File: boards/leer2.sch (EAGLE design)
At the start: 76 parts, among them IC2 7805DT, Q1 BC846BSMD, Q2 BC846BSMD, Q3 BC846BSMD, Q4 BC846BSMD, Q5 BC846BSMD, Q6 BC846BSMD, Q7 BC846BSMD, Q8 BC846BSMD

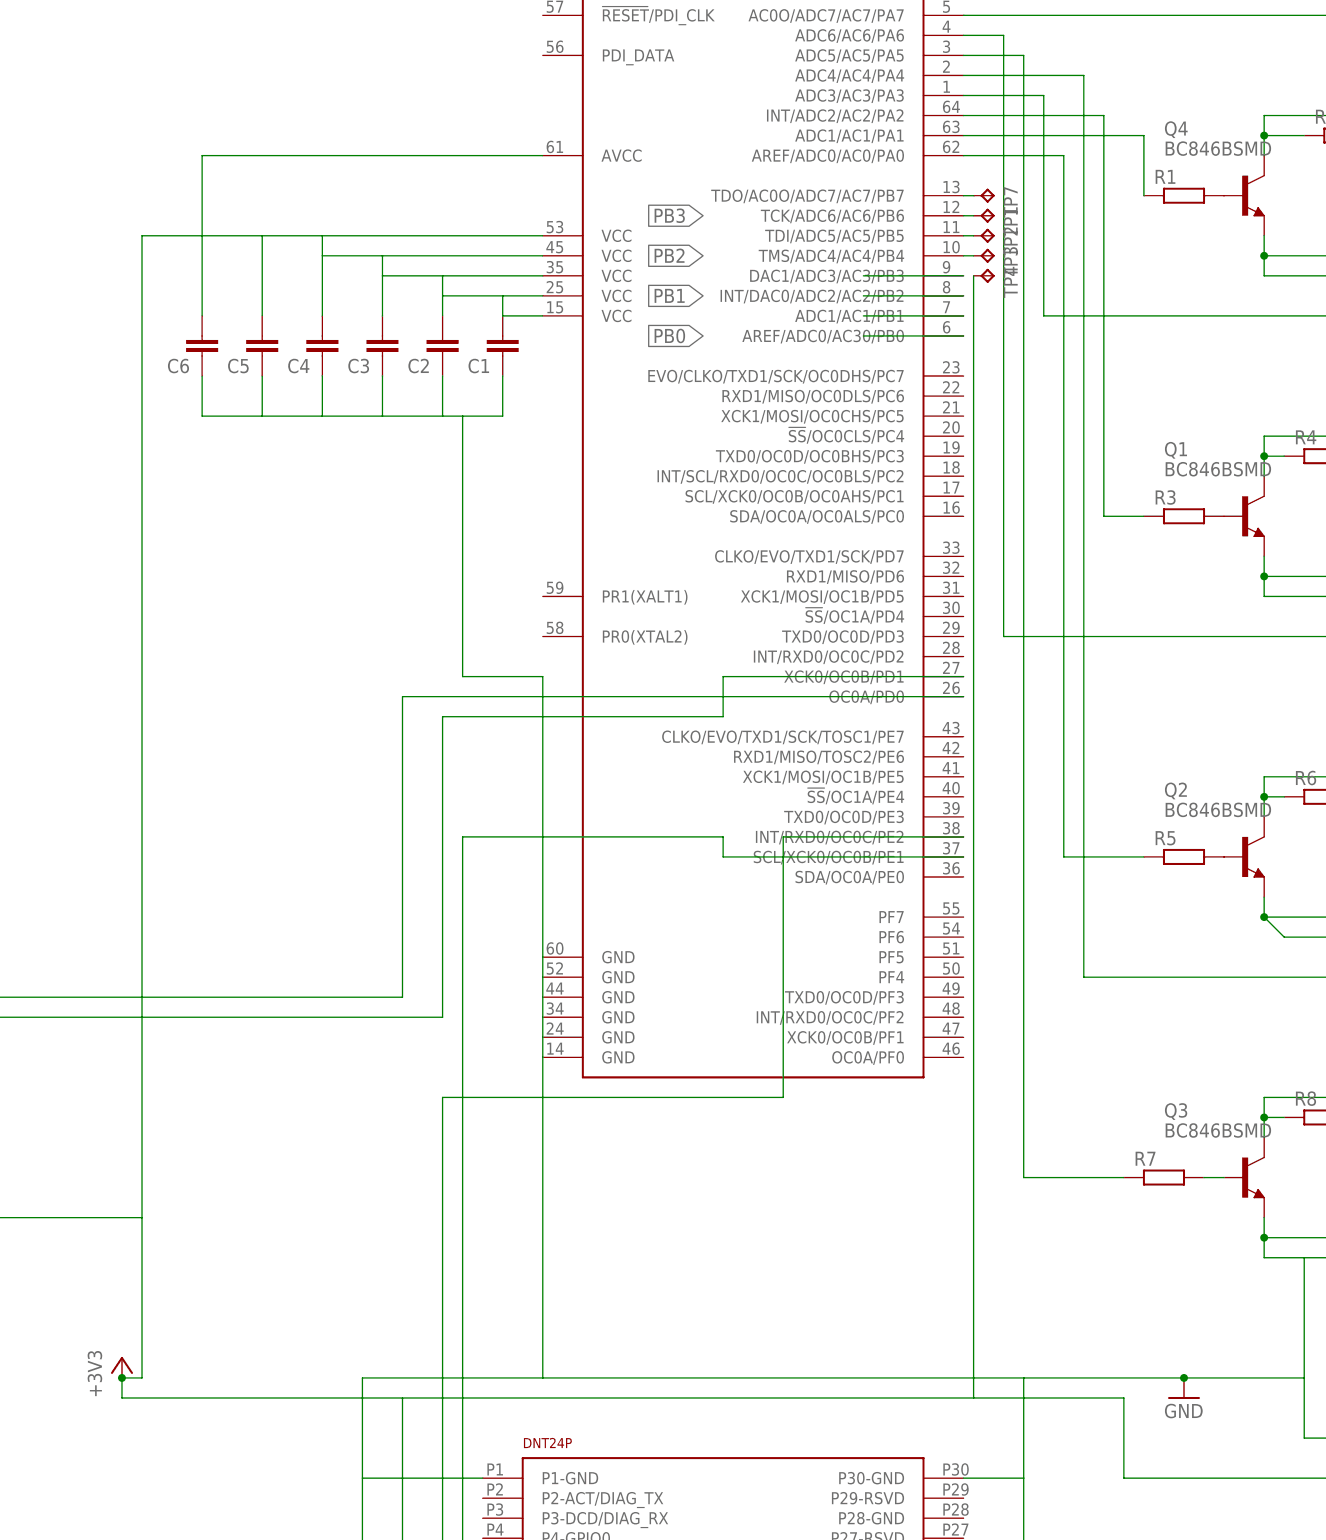
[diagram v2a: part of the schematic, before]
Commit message: Added Barometer
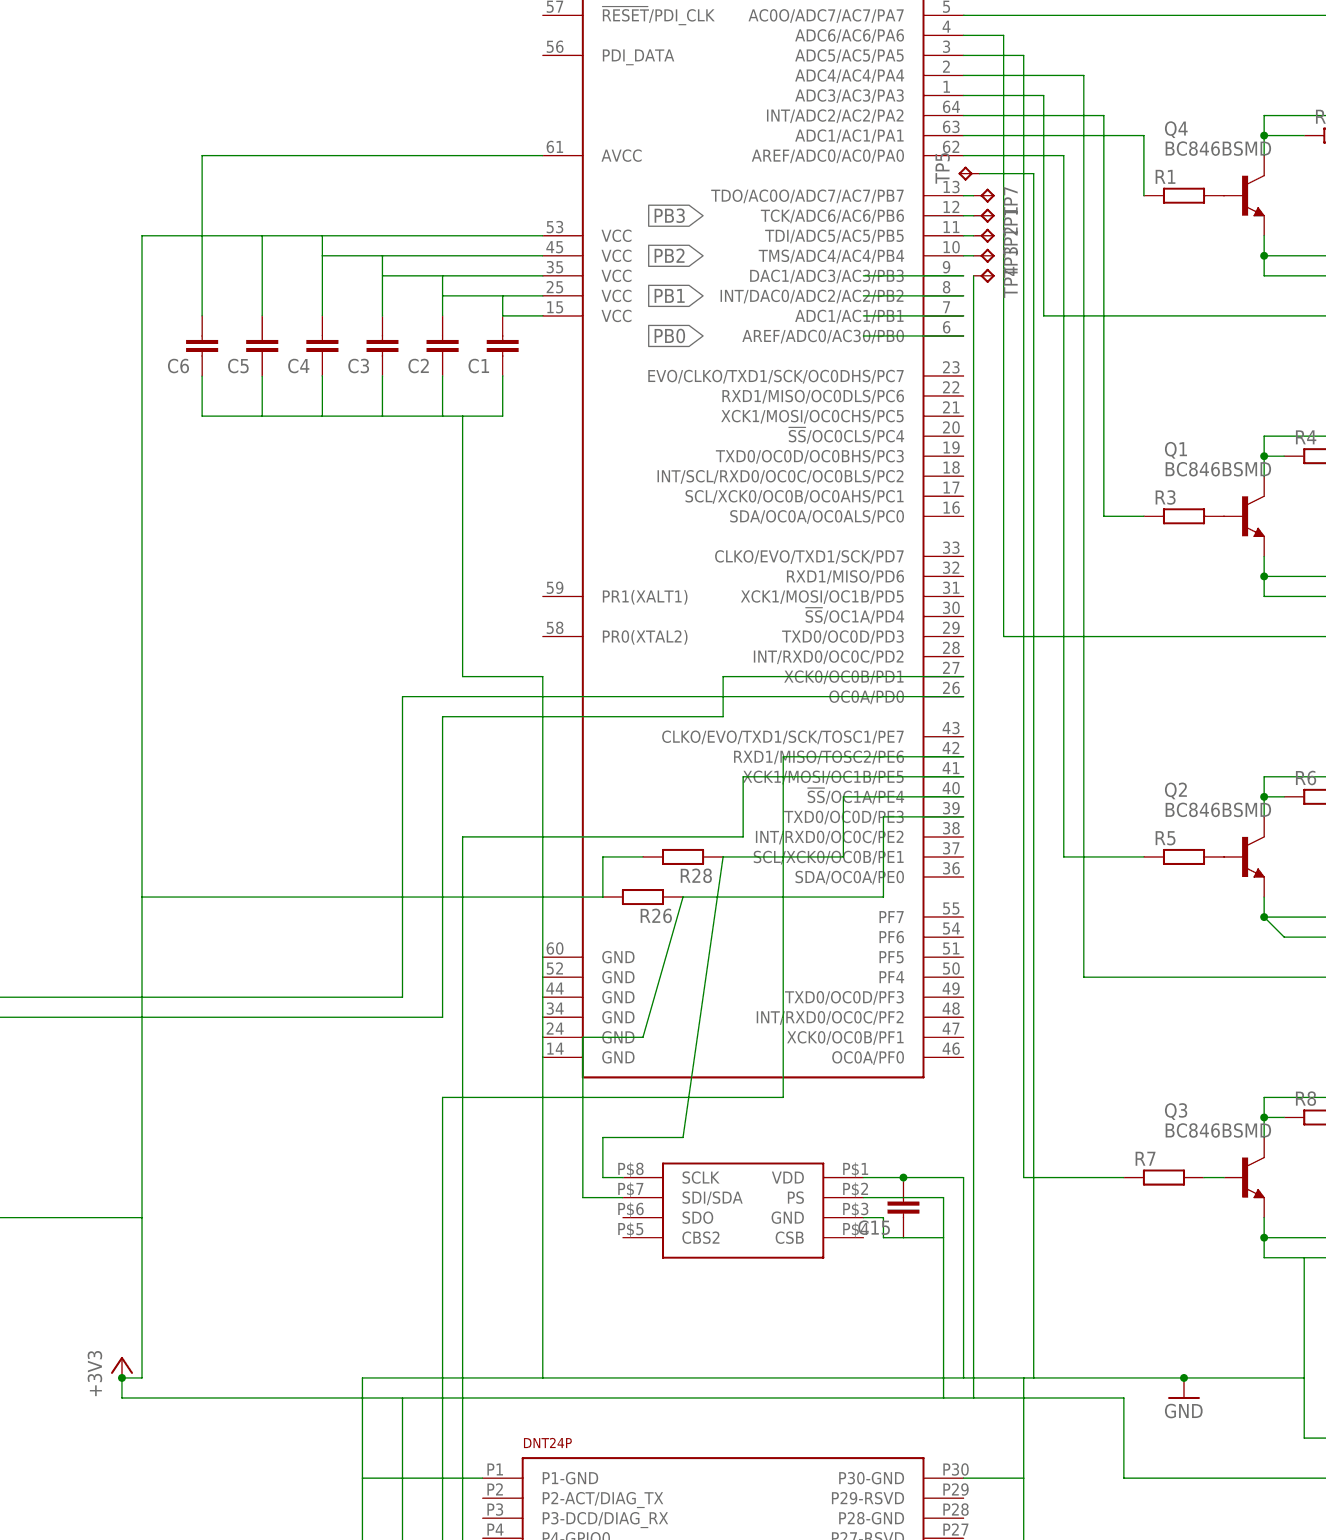
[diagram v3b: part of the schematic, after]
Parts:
- added C15: (no value), eagle-ltspice:CC0603
- added R26, R28: (no value), eagle-ltspice:RR0603
- added TP5: TPTP08R, testpad:TPTP08R
- added U$2: MS5611, ms5611:MS5611
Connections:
- new net N$46: IC3.!SS!/OC1A/PE4, R28.1, U$2.SCLK
- new net N$47: IC3.TXD0/OC0D/PE3, R26.1, U$2.SDI/SDA
- net +3V3: now also C15.1, R26.2, R28.2, U$2.GND, U$2.PS
- net GND: now also C15.2, TP5.TP, U$2.VDD
- net N$33: now also IC3.XCK1/MOSI/OC1B/PE5; no longer IC3.SCL/XCK0/OC0B/PE1
- net N$36: now also IC3.RXD1/MISO/TOSC2/PE6; no longer IC3.INT/RXD0/OC0C/PE2
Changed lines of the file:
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@@
 <?xml version="1.0" encoding="utf-8"?>
 <!DOCTYPE eagle SYSTEM "eagle.dtd">
-<eagle version="6.5.0">
+<eagle version="6.4">
 <drawing>
 <settings>
@@
 <layers>
 <layer number="1" name="Top" color="4" fill="1" visible="no" active="no"/>
+<layer number="2" name="Route2" color="1" fill="3" visible="no" active="no"/>
+<layer number="3" name="Route3" color="4" fill="3" visible="no" active="no"/>
+<layer number="4" name="Route4" color="1" fill="4" visible="no" active="no"/>
+<layer number="5" name="Route5" color="4" fill="4" visible="no" active="no"/>
+<layer number="6" name="Route6" color="1" fill="8" visible="no" active="no"/>
+<layer number="7" name="Route7" color="4" fill="8" visible="no" active="no"/>
+<layer number="8" name="Route8" color="1" fill="2" visible="no" active="no"/>
+<layer number="9" name="Route9" color="4" fill="2" visible="no" active="no"/>
+<layer number="10" name="Route10" color="1" fill="7" visible="no" active="no"/>
+<layer number="11" name="Route11" color="4" fill="7" visible="no" active="no"/>
+<layer number="12" name="Route12" color="1" fill="5" visible="no" active="no"/>
+<layer number="13" name="Route13" color="4" fill="5" visible="no" active="no"/>
+<layer number="14" name="Route14" color="1" fill="6" visible="no" active="no"/>
+<layer number="15" name="Route15" color="4" fill="6" visible="no" active="no"/>
 <layer number="16" name="Bottom" color="1" fill="1" visible="no" active="no"/>
 <layer number="17" name="Pads" color="2" fill="1" visible="no" active="no"/>
@@
 <part name="C8" library="eagle-ltspice" deviceset="C" device="C0603"/>
 <part name="C11" library="eagle-ltspice" deviceset="C" device="C0603"/>
+<part name="TP5" library="testpad" deviceset="TP" device="TP08R"/>
+<part name="U$2" library="ms5611" deviceset="MS5611" device=""/>
+<part name="C15" library="eagle-ltspice" deviceset="C" device="C0603"/>
+<part name="R26" library="eagle-ltspice" deviceset="R" device="R0603"/>
+<part name="R28" library="eagle-ltspice" deviceset="R" device="R0603"/>
 </parts>
 <sheets>
@@
 <instance part="C8" gate="G$1" x="104.14" y="215.9" rot="R180"/>
 <instance part="C11" gate="G$1" x="114.3" y="215.9" rot="R180"/>
+<instance part="TP5" gate="G$1" x="261.112" y="221.234" rot="R90"/>
+<instance part="U$2" gate="G$1" x="231.14" y="83.82"/>
+<instance part="C15" gate="G$1" x="254" y="88.9" rot="R180"/>
+<instance part="R26" gate="G$1" x="220.98" y="129.54" rot="R180"/>
+<instance part="R28" gate="G$1" x="226.06" y="134.62" rot="R180"/>
 </instances>
 <busses>
@@
 <wire x1="200.66" y1="45.72" x2="198.12" y2="45.72" width="0.1524" layer="91"/>
 <wire x1="198.12" y1="45.72" x2="198.12" y2="137.16" width="0.1524" layer="91"/>
-<wire x1="198.12" y1="137.16" x2="231.14" y2="137.16" width="0.1524" layer="91"/>
-<wire x1="231.14" y1="137.16" x2="231.14" y2="134.62" width="0.1524" layer="91"/>
-<pinref part="IC3" gate="G$1" pin="SCL/XCK0/OC0B/PE1"/>
-<wire x1="231.14" y1="134.62" x2="261.62" y2="134.62" width="0.1524" layer="91"/>
+<wire x1="198.12" y1="137.16" x2="233.68" y2="137.16" width="0.1524" layer="91"/>
+<wire x1="233.68" y1="137.16" x2="233.68" y2="144.78" width="0.1524" layer="91"/>
+<pinref part="IC3" gate="G$1" pin="XCK1/MOSI/OC1B/PE5"/>
+<wire x1="233.68" y1="144.78" x2="261.62" y2="144.78" width="0.1524" layer="91"/>
 </segment>
 </net>
@@
 <wire x1="195.58" y1="43.18" x2="195.58" y2="104.14" width="0.1524" layer="91"/>
 <wire x1="195.58" y1="104.14" x2="238.76" y2="104.14" width="0.1524" layer="91"/>
-<wire x1="238.76" y1="104.14" x2="238.76" y2="137.16" width="0.1524" layer="91"/>
-<pinref part="IC3" gate="G$1" pin="INT/RXD0/OC0C/PE2"/>
-<wire x1="238.76" y1="137.16" x2="261.62" y2="137.16" width="0.1524" layer="91"/>
+<wire x1="238.76" y1="104.14" x2="238.76" y2="147.32" width="0.1524" layer="91"/>
+<pinref part="IC3" gate="G$1" pin="RXD1/MISO/TOSC2/PE6"/>
+<wire x1="238.76" y1="147.32" x2="261.62" y2="147.32" width="0.1524" layer="91"/>
 </segment>
 </net>
@@
 <wire x1="281.94" y1="55.88" x2="281.94" y2="66.04" width="0.1524" layer="91"/>
 <wire x1="281.94" y1="66.04" x2="262.89" y2="66.04" width="0.1524" layer="91"/>
-<wire x1="262.89" y1="66.04" x2="190.5" y2="66.04" width="0.1524" layer="91"/>
+<wire x1="262.89" y1="66.04" x2="259.08" y2="66.04" width="0.1524" layer="91"/>
+<wire x1="259.08" y1="66.04" x2="190.5" y2="66.04" width="0.1524" layer="91"/>
 <wire x1="190.5" y1="66.04" x2="154.94" y2="66.04" width="0.1524" layer="91"/>
 <wire x1="154.94" y1="66.04" x2="154.94" y2="68.58" width="0.1524" layer="91"/>
 <wire x1="154.94" y1="68.58" x2="157.48" y2="68.58" width="0.1524" layer="91"/>
 <wire x1="157.48" y1="68.58" x2="157.48" y2="88.9" width="0.1524" layer="91"/>
-<wire x1="157.48" y1="88.9" x2="157.48" y2="213.36" width="0.1524" layer="91"/>
+<wire x1="157.48" y1="88.9" x2="157.48" y2="129.54" width="0.1524" layer="91"/>
+<wire x1="157.48" y1="129.54" x2="157.48" y2="213.36" width="0.1524" layer="91"/>
 <wire x1="193.04" y1="25.4" x2="190.5" y2="25.4" width="0.1524" layer="91"/>
 <wire x1="190.5" y1="25.4" x2="190.5" y2="66.04" width="0.1524" layer="91"/>
@@
 <wire x1="262.89" y1="66.04" x2="262.89" y2="208.28" width="0.1524" layer="91"/>
 <pinref part="TP4" gate="G$1" pin="TP"/>
+<pinref part="U$2" gate="G$1" pin="PS"/>
+<wire x1="248.92" y1="91.44" x2="259.08" y2="91.44" width="0.1524" layer="91"/>
+<wire x1="259.08" y1="91.44" x2="259.08" y2="86.36" width="0.1524" layer="91"/>
+<pinref part="U$2" gate="G$1" pin="GND"/>
+<wire x1="259.08" y1="86.36" x2="259.08" y2="66.04" width="0.1524" layer="91"/>
+<wire x1="248.92" y1="88.9" x2="251.46" y2="88.9" width="0.1524" layer="91"/>
+<wire x1="251.46" y1="88.9" x2="251.46" y2="86.36" width="0.1524" layer="91"/>
+<pinref part="C15" gate="G$1" pin="1"/>
+<wire x1="251.46" y1="86.36" x2="254" y2="86.36" width="0.1524" layer="91"/>
+<wire x1="259.08" y1="86.36" x2="254" y2="86.36" width="0.1524" layer="91"/>
+<pinref part="R28" gate="G$1" pin="2"/>
+<pinref part="R26" gate="G$1" pin="2"/>
+<wire x1="220.98" y1="134.62" x2="215.9" y2="134.62" width="0.1524" layer="91"/>
+<wire x1="215.9" y1="134.62" x2="215.9" y2="129.54" width="0.1524" layer="91"/>
+<wire x1="157.48" y1="129.54" x2="215.9" y2="129.54" width="0.1524" layer="91"/>
 </segment>
 </net>
@@
 <wire x1="304.8" y1="68.58" x2="304.8" y2="83.82" width="0.1524" layer="91"/>
 <wire x1="304.8" y1="68.58" x2="289.56" y2="68.58" width="0.1524" layer="91"/>
-<wire x1="289.56" y1="68.58" x2="269.24" y2="68.58" width="0.1524" layer="91"/>
-<wire x1="269.24" y1="68.58" x2="208.28" y2="68.58" width="0.1524" layer="91"/>
+<wire x1="289.56" y1="68.58" x2="270.51" y2="68.58" width="0.1524" layer="91"/>
+<wire x1="270.51" y1="68.58" x2="269.24" y2="68.58" width="0.1524" layer="91"/>
+<wire x1="269.24" y1="68.58" x2="261.62" y2="68.58" width="0.1524" layer="91"/>
+<wire x1="261.62" y1="68.58" x2="208.28" y2="68.58" width="0.1524" layer="91"/>
 <wire x1="208.28" y1="68.58" x2="185.42" y2="68.58" width="0.1524" layer="91"/>
 <pinref part="U$1" gate="G$1" pin="P1-GND"/>
@@
 <wire x1="172.72" y1="190.5" x2="165.1" y2="190.5" width="0.1524" layer="91"/>
 <wire x1="165.1" y1="190.5" x2="165.1" y2="195.58" width="0.1524" layer="91"/>
+<wire x1="270.51" y1="68.58" x2="270.51" y2="221.234" width="0.1524" layer="91"/>
+<wire x1="270.51" y1="221.234" x2="263.652" y2="221.234" width="0.1524" layer="91"/>
+<pinref part="TP5" gate="G$1" pin="TP"/>
+<pinref part="U$2" gate="G$1" pin="VDD"/>
+<wire x1="248.92" y1="93.98" x2="254" y2="93.98" width="0.1524" layer="91"/>
+<wire x1="254" y1="93.98" x2="261.62" y2="93.98" width="0.1524" layer="91"/>
+<wire x1="261.62" y1="93.98" x2="261.62" y2="68.58" width="0.1524" layer="91"/>
+<pinref part="C15" gate="G$1" pin="2"/>
+<junction x="254" y="93.98"/>
 </segment>
 <segment>
@@
 </segment>
 </net>
+<net name="N$46" class="0">
+<segment>
+<wire x1="231.14" y1="134.62" x2="226.06" y2="99.06" width="0.1524" layer="91"/>
+<wire x1="226.06" y1="99.06" x2="215.9" y2="99.06" width="0.1524" layer="91"/>
+<wire x1="215.9" y1="99.06" x2="215.9" y2="93.98" width="0.1524" layer="91"/>
+<pinref part="U$2" gate="G$1" pin="SCLK"/>
+<wire x1="215.9" y1="93.98" x2="218.44" y2="93.98" width="0.1524" layer="91"/>
+<pinref part="R28" gate="G$1" pin="1"/>
+<wire x1="231.14" y1="134.62" x2="246.38" y2="134.62" width="0.1524" layer="91"/>
+<wire x1="246.38" y1="134.62" x2="246.38" y2="142.24" width="0.1524" layer="91"/>
+<pinref part="IC3" gate="G$1" pin="!SS!/OC1A/PE4"/>
+<wire x1="246.38" y1="142.24" x2="261.62" y2="142.24" width="0.1524" layer="91"/>
+</segment>
+</net>
+<net name="N$47" class="0">
+<segment>
+<pinref part="U$2" gate="G$1" pin="SDI/SDA"/>
+<wire x1="218.44" y1="91.44" x2="213.36" y2="91.44" width="0.1524" layer="91"/>
+<wire x1="213.36" y1="91.44" x2="213.36" y2="111.76" width="0.1524" layer="91"/>
+<wire x1="213.36" y1="111.76" x2="220.98" y2="111.76" width="0.1524" layer="91"/>
+<wire x1="220.98" y1="111.76" x2="226.06" y2="129.54" width="0.1524" layer="91"/>
+<pinref part="R26" gate="G$1" pin="1"/>
+<wire x1="226.06" y1="129.54" x2="251.46" y2="129.54" width="0.1524" layer="91"/>
+<wire x1="251.46" y1="129.54" x2="251.46" y2="139.7" width="0.1524" layer="91"/>
+<pinref part="IC3" gate="G$1" pin="TXD0/OC0D/PE3"/>
+<wire x1="251.46" y1="139.7" x2="261.62" y2="139.7" width="0.1524" layer="91"/>
+</segment>
+</net>

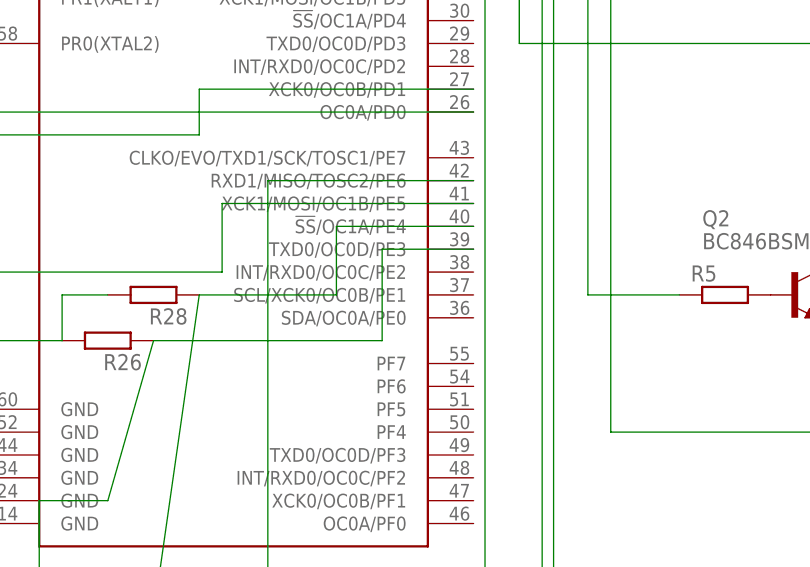
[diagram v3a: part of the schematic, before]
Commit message: Changed location of barometer
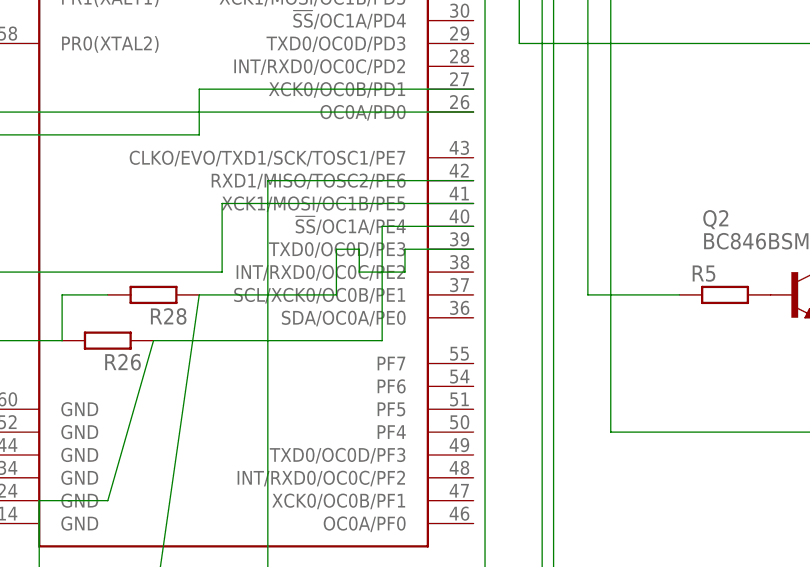
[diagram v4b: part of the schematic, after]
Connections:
- net N$46: now also IC3.TXD0/OC0D/PE3; no longer IC3.!SS!/OC1A/PE4
- net N$47: now also IC3.!SS!/OC1A/PE4; no longer IC3.TXD0/OC0D/PE3
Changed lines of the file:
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@@
 <?xml version="1.0" encoding="utf-8"?>
 <!DOCTYPE eagle SYSTEM "eagle.dtd">
-<eagle version="6.4">
+<eagle version="6.5.0">
 <drawing>
 <settings>
@@
 <pinref part="R28" gate="G$1" pin="1"/>
 <wire x1="231.14" y1="134.62" x2="246.38" y2="134.62" width="0.1524" layer="91"/>
-<wire x1="246.38" y1="134.62" x2="246.38" y2="142.24" width="0.1524" layer="91"/>
-<pinref part="IC3" gate="G$1" pin="!SS!/OC1A/PE4"/>
-<wire x1="246.38" y1="142.24" x2="261.62" y2="142.24" width="0.1524" layer="91"/>
+<wire x1="246.38" y1="134.62" x2="246.38" y2="139.7" width="0.1524" layer="91"/>
+<wire x1="246.38" y1="139.7" x2="248.92" y2="139.7" width="0.1524" layer="91"/>
+<wire x1="248.92" y1="139.7" x2="248.92" y2="137.16" width="0.1524" layer="91"/>
+<wire x1="248.92" y1="137.16" x2="254" y2="137.16" width="0.1524" layer="91"/>
+<wire x1="254" y1="137.16" x2="254" y2="139.7" width="0.1524" layer="91"/>
+<pinref part="IC3" gate="G$1" pin="TXD0/OC0D/PE3"/>
+<wire x1="254" y1="139.7" x2="261.62" y2="139.7" width="0.1524" layer="91"/>
 </segment>
 </net>
@@
 <pinref part="R26" gate="G$1" pin="1"/>
 <wire x1="226.06" y1="129.54" x2="251.46" y2="129.54" width="0.1524" layer="91"/>
-<wire x1="251.46" y1="129.54" x2="251.46" y2="139.7" width="0.1524" layer="91"/>
-<pinref part="IC3" gate="G$1" pin="TXD0/OC0D/PE3"/>
-<wire x1="251.46" y1="139.7" x2="261.62" y2="139.7" width="0.1524" layer="91"/>
-</segment>
-</net>
+<wire x1="251.46" y1="129.54" x2="251.46" y2="142.24" width="0.1524" layer="91"/>
+<pinref part="IC3" gate="G$1" pin="!SS!/OC1A/PE4"/>
+<wire x1="251.46" y1="142.24" x2="261.62" y2="142.24" width="0.1524" layer="91"/>
+</segment>
+</net>
